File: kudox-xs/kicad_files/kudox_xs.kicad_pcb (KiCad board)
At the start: 2 copper layers, 91.1 x 77.3 mm, 39 parts, among them K0 KEYSW, K1 KEYSW, K10 KEYSW, K11 KEYSW, K12 KEYSW, K13 KEYSW, K2 KEYSW, K20 KEYSW, K21 KEYSW, K22 KEYSW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

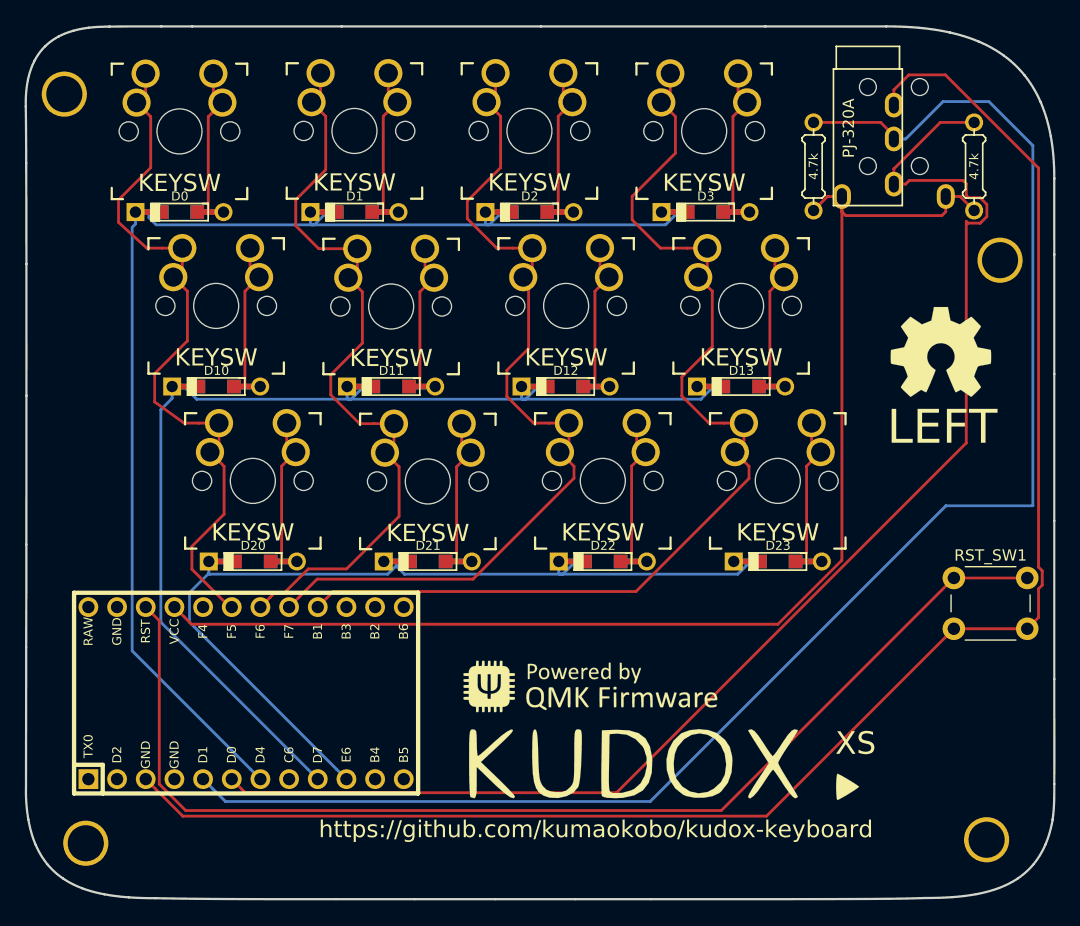
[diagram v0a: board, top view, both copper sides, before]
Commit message: Add filled zones.
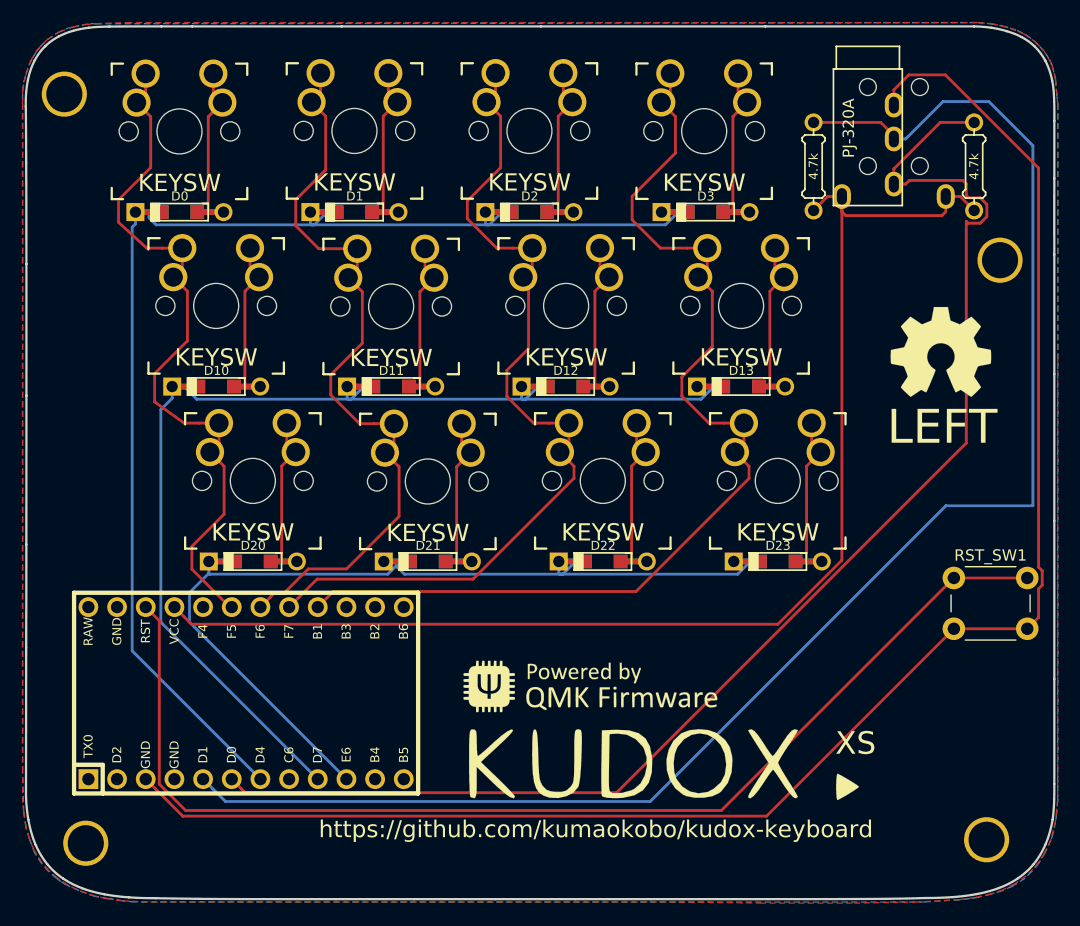
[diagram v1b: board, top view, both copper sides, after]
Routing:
- added copper zone on B.Cu, net (none)
- added copper zone on F.Cu, net (none)
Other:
- outline, holes or cut-outs redrawn
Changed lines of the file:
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@@
-(kicad_pcb (version 20171130) (host pcbnew "(6.0.0-rc1-dev-1469-g932b9a334)")
+(kicad_pcb (version 20171130) (host pcbnew "(5.1.2-1)-1")
   (general
     (thickness 1.6)
@@
       (xy -9.943822 1.795852)) (layer B.SilkS) (width 0.01))
   )
+  (gr_curve (pts (xy 172.9 59.06) (xy 172.91401 56.94942) (xy 172.846323 56.178696) (xy 172.709099 55.503622)) (layer Edge.Cuts) (width 0.2))
+  (gr_curve (pts (xy 172.709099 55.503622) (xy 172.571875 54.828548) (xy 172.365113 54.249124) (xy 172.103885 53.751799)) (layer Edge.Cuts) (width 0.2))
+  (gr_curve (pts (xy 172.103885 53.751799) (xy 171.842657 53.254474) (xy 171.526962 52.839248) (xy 171.171871 52.492568)) (layer Edge.Cuts) (width 0.2))
+  (gr_curve (pts (xy 171.171871 52.492568) (xy 170.816781 52.145889) (xy 170.422294 51.867757) (xy 170.003483 51.64462)) (layer Edge.Cuts) (width 0.2))
+  (gr_curve (pts (xy 170.003483 51.64462) (xy 169.584672 51.421484) (xy 169.141535 51.253342) (xy 168.689145 51.126645)) (layer Edge.Cuts) (width 0.2))
+  (gr_curve (pts (xy 168.689145 51.126645) (xy 168.26 50.99) (xy 167.78 50.89) (xy 167.35 50.82)) (layer Edge.Cuts) (width 0.2))
+  (gr_curve (pts (xy 167.35 50.82) (xy 166.85 50.76) (xy 166.49 50.71) (xy 165.8 50.699453)) (layer Edge.Cuts) (width 0.2))
   (gr_line (start 141.9 97.5) (end 141.9 84.5) (layer Eco1.User) (width 0.15))
   (gr_line (start 155.9 83.5) (end 155.9 98.5) (layer Dwgs.User) (width 0.15))
@@
   (gr_curve (pts (xy 169.683322 126.162704) (xy 170.197984 125.812743) (xy 170.66148 125.39701) (xy 171.067205 124.90449)) (layer Edge.Cuts) (width 0.2))
   (gr_curve (pts (xy 171.067205 124.90449) (xy 171.472931 124.411971) (xy 171.820887 123.842665) (xy 172.10447 123.18556)) (layer Edge.Cuts) (width 0.2))
-  (gr_curve (pts (xy 172.10447 123.18556) (xy 172.388053 122.528454) (xy 172.607263 121.783549) (xy 172.755498 120.93983)) (layer Edge.Cuts) (width 0.2))
+  (gr_curve (pts (xy 172.10447 123.18556) (xy 172.388053 122.528454) (xy 172.607263 121.783549) (xy 172.745992 120.970193)) (layer Edge.Cuts) (width 0.2))
   (gr_text XS (at 125.1 114.21) (layer B.SilkS)
     (effects (font (size 2 2) (thickness 0.3)) (justify mirror))
@@
   (gr_curve (pts (xy 81.820416 105.686274) (xy 81.835221 100.06) (xy 81.835221 98.96) (xy 81.835221 96.595652)) (layer Edge.Cuts) (width 0.2))
   (gr_curve (pts (xy 81.803686 118.274178) (xy 81.809071 114.363015) (xy 81.814904 110.099871) (xy 81.820416 105.686274)) (layer Edge.Cuts) (width 0.2))
-  (gr_curve (pts (xy 82.011773 120.957947) (xy 81.863538 120.114228) (xy 81.786279 119.171696) (xy 81.8 118.28)) (layer Edge.Cuts) (width 0.2))
+  (gr_curve (pts (xy 82.011773 120.957947) (xy 81.863538 120.114228) (xy 81.786279 119.171696) (xy 81.803686 118.274178)) (layer Edge.Cuts) (width 0.2))
   (gr_curve (pts (xy 82.662801 123.203677) (xy 82.379218 122.546571) (xy 82.160008 121.801666) (xy 82.011773 120.957947)) (layer Edge.Cuts) (width 0.2))
   (gr_curve (pts (xy 83.700066 124.922607) (xy 83.29434 124.430088) (xy 82.946384 123.860782) (xy 82.662801 123.203677)) (layer Edge.Cuts) (width 0.2))
@@
   (gr_curve (pts (xy 172.895992 81.495039) (xy 172.895992 85.502473) (xy 172.895992 89.914081) (xy 172.895992 94.495994)) (layer Edge.Cuts) (width 0.2))
   (gr_curve (pts (xy 172.895992 70.919129) (xy 172.895992 73.884346) (xy 172.895992 77.487606) (xy 172.895992 81.495039)) (layer Edge.Cuts) (width 0.2))
-  (gr_curve (pts (xy 172.891984 64.171474) (xy 172.890437 65.626738) (xy 172.892164 67.953912) (xy 172.896273 70.919129)) (layer Edge.Cuts) (width 0.2))
-  (gr_curve (pts (xy 172.582085 60.429541) (xy 172.788777 61.562322) (xy 172.897475 62.820181) (xy 172.895992 64.215737)) (layer Edge.Cuts) (width 0.2))
-  (gr_curve (pts (xy 171.680213 57.393816) (xy 172.070707 58.289058) (xy 172.375393 59.296761) (xy 172.582085 60.429541)) (layer Edge.Cuts) (width 0.2))
-  (gr_curve (pts (xy 170.263498 55.032848) (xy 170.813419 55.71579) (xy 171.28972 56.498573) (xy 171.680213 57.393816)) (layer Edge.Cuts) (width 0.2))
-  (gr_curve (pts (xy 168.405059 53.270926) (xy 169.090034 53.766805) (xy 169.713576 54.349906) (xy 170.263498 55.032848)) (layer Edge.Cuts) (width 0.2))
-  (gr_curve (pts (xy 166.178018 52.032338) (xy 166.973674 52.366391) (xy 167.720083 52.775048) (xy 168.405059 53.270926)) (layer Edge.Cuts) (width 0.2))
-  (gr_curve (pts (xy 163.655495 51.241371) (xy 164.537458 51.438836) (xy 165.382361 51.698285) (xy 166.178018 52.032338)) (layer Edge.Cuts) (width 0.2))
-  (gr_curve (pts (xy 160.910611 50.822314) (xy 161.854508 50.908427) (xy 162.773531 51.043907) (xy 163.655495 51.241371)) (layer Edge.Cuts) (width 0.2))
-  (gr_curve (pts (xy 158.016487 50.699453) (xy 158.997944 50.699453) (xy 159.966714 50.7362) (xy 160.910611 50.822314)) (layer Edge.Cuts) (width 0.2))
-  (gr_curve (pts (xy 147.305545 50.699453) (xy 154.063878 50.699453) (xy 156.829614 50.699453) (xy 158.016487 50.699453)) (layer Edge.Cuts) (width 0.2))
+  (gr_curve (pts (xy 172.9 64.16) (xy 172.890437 65.626738) (xy 172.892164 67.953912) (xy 172.896273 70.919129)) (layer Edge.Cuts) (width 0.2))
+  (gr_curve (pts (xy 172.9 59.06) (xy 172.9 61.46) (xy 172.9 62.820181) (xy 172.9 64.16)) (layer Edge.Cuts) (width 0.2))
+  (gr_curve (pts (xy 147.305545 50.699453) (xy 154.063878 50.699453) (xy 156.829614 50.699453) (xy 165.8 50.699453)) (layer Edge.Cuts) (width 0.2))
   (gr_curve (pts (xy 127.417512 50.699453) (xy 133.796283 50.699453) (xy 140.547212 50.699453) (xy 147.305545 50.699453)) (layer Edge.Cuts) (width 0.2))
   (gr_curve (pts (xy 109.762437 50.699453) (xy 115.032132 50.699453) (xy 121.038742 50.699453) (xy 127.417512 50.699453)) (layer Edge.Cuts) (width 0.2))
@@
   (segment (start 143.4 120.16) (end 164 99.56) (width 0.25) (layer F.Cu) (net 30))
   (segment (start 95.952074 120.16) (end 143.4 120.16) (width 0.25) (layer F.Cu) (net 30))
+  (zone (net 0) (net_name "") (layer F.Cu) (hatch edge 0.508)
+    (connect_pads (clearance 0.508))
+    (min_thickness 0.254)
+    (fill yes (arc_segments 32) (thermal_gap 0.508) (thermal_bridge_width 0.508))
+    (polygon
+      (pts
+        (xy 173.2 57.56) (xy 173.2 80.26) (xy 173.2 116.66) (xy 173.2 119.16) (xy 173.1 120.16)
+        (xy 173 121.06) (xy 172.6 122.76) (xy 172 123.96) (xy 171.5 124.76) (xy 171 125.36)
+        (xy 170.4 125.96) (xy 169.4 126.66) (xy 168.4 127.16) (xy 167.3 127.56) (xy 165.9 127.86)
+        (xy 164.5 128.06) (xy 160.8 128.26) (xy 155 128.36) (xy 147 128.36) (xy 139.4 128.26)
+        (xy 92.6 128.26) (xy 90.3 128.16) (xy 88.9 127.96) (xy 88 127.76) (xy 87.1 127.46)
+        (xy 86.3 127.16) (xy 85.5 126.76) (xy 84.6 126.16) (xy 83.8 125.46) (xy 83.2 124.76)
+        (xy 82.5 123.66) (xy 82.1 122.66) (xy 81.8 121.66) (xy 81.6 120.26) (xy 81.5 119.46)
+        (xy 81.5 116.76) (xy 81.5 57.56) (xy 81.5 56.36) (xy 81.8 54.86) (xy 82.2 53.76)
+        (xy 82.8 52.76) (xy 83.7 51.86) (xy 84.8 51.16) (xy 85.9 50.76) (xy 87 50.56)
+        (xy 88 50.46) (xy 90.7 50.36) (xy 166.2 50.36) (xy 167.4 50.46) (xy 169 50.86)
+        (xy 170.2 51.36) (xy 171.2 52.06) (xy 171.9 52.76) (xy 172.7 54.06) (xy 173 55.36)
+      )
+    )
+  )
+  (zone (net 0) (net_name "") (layer B.Cu) (hatch edge 0.508)
+    (connect_pads (clearance 0.508))
+    (min_thickness 0.254)
+    (fill yes (arc_segments 32) (thermal_gap 0.508) (thermal_bridge_width 0.508))
+    (polygon
+      (pts
+        (xy 173 55.46) (xy 173.1 56.56) (xy 173.2 57.56) (xy 173.2 119.26) (xy 173.1 120.46)
+        (xy 173 121.16) (xy 172.8 122.16) (xy 172.6 122.76) (xy 172.1 123.86) (xy 171.5 124.86)
+        (xy 170.9 125.56) (xy 170.3 126.16) (xy 169.2 126.86) (xy 168.3 127.26) (xy 167.3 127.56)
+        (xy 166.1 127.86) (xy 165.4 127.96) (xy 164.5 128.06) (xy 161.4 128.26) (xy 91.4 128.26)
+        (xy 90.4 128.16) (xy 89.1 127.96) (xy 87.9 127.76) (xy 86.5 127.26) (xy 85.4 126.76)
+        (xy 84.9 126.46) (xy 84.5 126.16) (xy 83.8 125.56) (xy 83.2 124.86) (xy 82.6 123.96)
+        (xy 82.1 122.66) (xy 81.8 121.66) (xy 81.6 120.26) (xy 81.5 116.76) (xy 81.5 56.46)
+        (xy 81.6 55.66) (xy 81.8 54.96) (xy 82.1 54.06) (xy 82.4 53.46) (xy 82.7 52.96)
+        (xy 83.1 52.46) (xy 83.7 51.86) (xy 84.6 51.26) (xy 85.5 50.86) (xy 86 50.76)
+        (xy 86.8 50.56) (xy 87.5 50.46) (xy 88 50.46) (xy 166.1 50.36) (xy 167.2 50.46)
+        (xy 168.3 50.66) (xy 169 50.86) (xy 169.6 51.06) (xy 170.4 51.46) (xy 171.1 51.96)
+        (xy 171.6 52.46) (xy 172.1 53.06) (xy 172.5 53.66) (xy 172.7 54.26) (xy 172.9 54.86)
+      )
+    )
+  )
 )
